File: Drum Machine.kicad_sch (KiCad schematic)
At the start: 20 parts

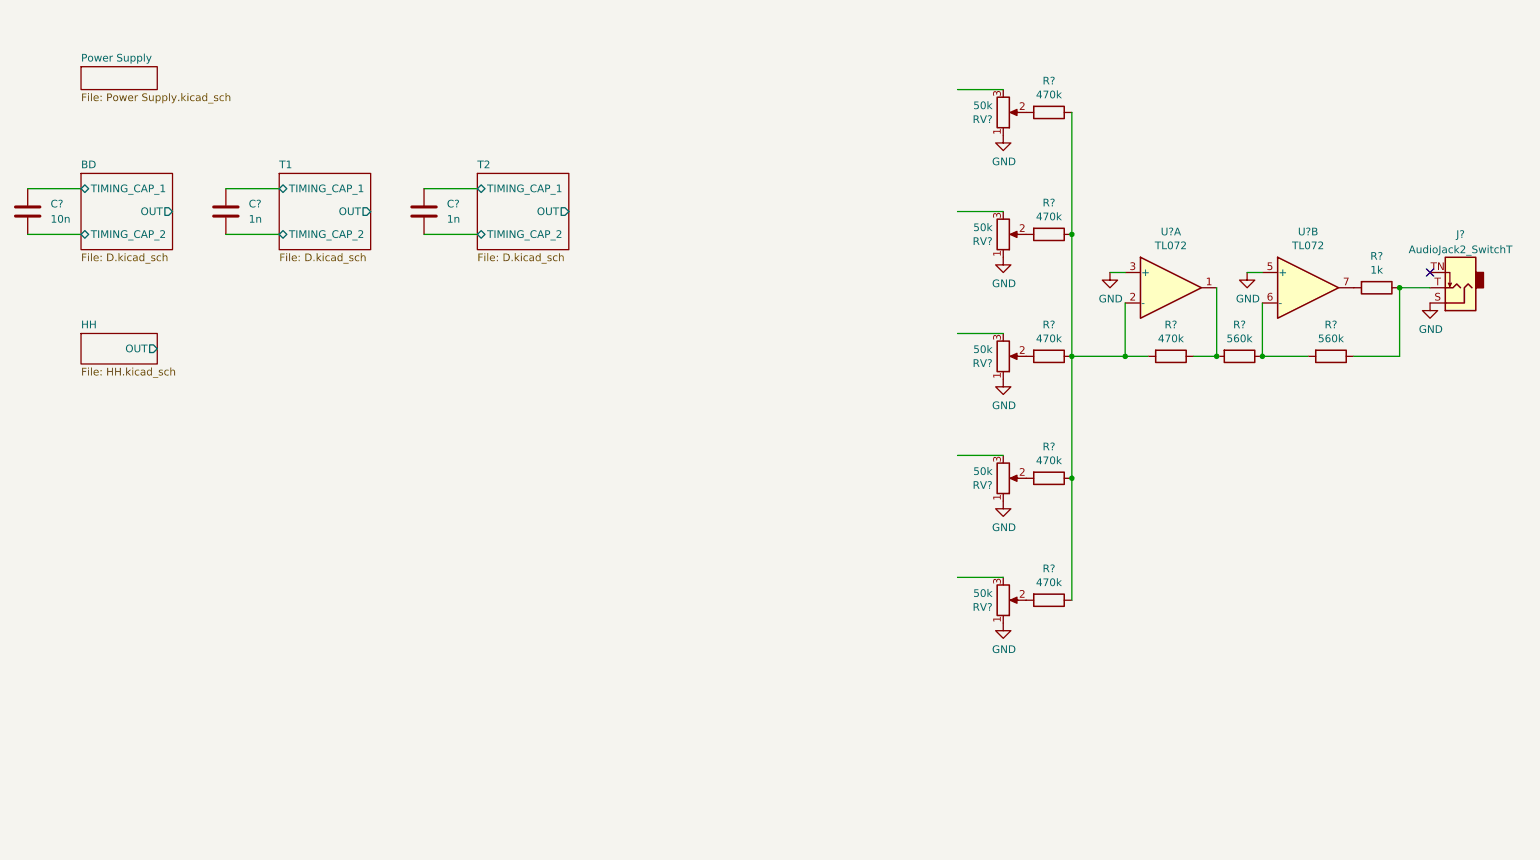
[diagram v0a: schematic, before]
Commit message: Finish schematic
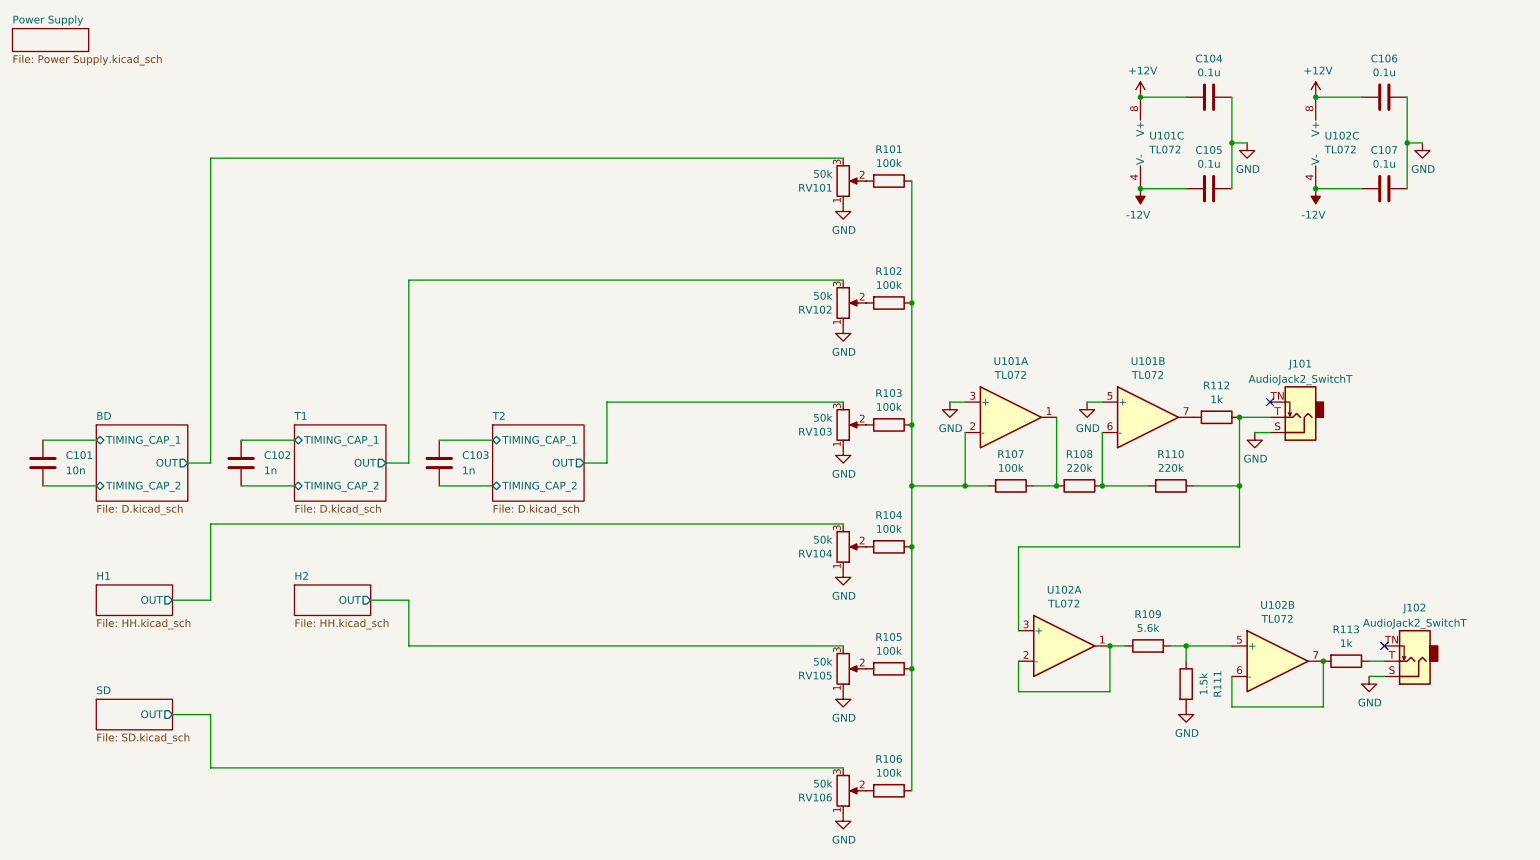
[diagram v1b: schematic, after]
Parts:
- removed R?: 1k, Resistor_THT:R_Axial_DIN0207_L6.3mm_D2.5mm_P7.62mm_Horizontal, symbol Device:R
- added C104, C105, C106, C107: 0.1u, Capacitor_THT:C_Disc_D5.0mm_W2.5mm_P5.00mm, symbol Device:C
- added J102: AudioJack2_SwitchT, Connector_Audio:Jack_3.5mm_QingPu_WQP-PJ398SM_Vertical_CircularHoles, symbol Connector:AudioJack2_SwitchT
- added R106: 100k, Resistor_THT:R_Axial_DIN0207_L6.3mm_D2.5mm_P7.62mm_Horizontal, symbol Device:R
- added R109: 5.6k, Resistor_THT:R_Axial_DIN0207_L6.3mm_D2.5mm_P7.62mm_Horizontal, symbol Device:R
- added R111: 1.5k, Resistor_THT:R_Axial_DIN0207_L6.3mm_D2.5mm_P7.62mm_Horizontal, symbol Device:R
- added R112, R113: 1k, Resistor_THT:R_Axial_DIN0207_L6.3mm_D2.5mm_P7.62mm_Horizontal, symbol Device:R
- added RV106: 50k, Potentiometer_THT:Potentiometer_Alpha_RD901F-40-00D_Single_Vertical_CircularHoles, symbol Device:R_Potentiometer
- added unit 3 of U101
- added U102: TL072, Package_DIP:DIP-8_W7.62mm_Socket, symbol Amplifier_Operational:TL072
- C101, C102, C103: renamed from C?; footprint (none) -> Capacitor_THT:C_Disc_D5.0mm_W2.5mm_P5.00mm
- R101, R102, R103, R104, R105, R107: renamed from R?; value 470k -> 100k
- R108, R110: renamed from R?; value 560k -> 220k
- gave numbers to parts that had none: 7
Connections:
- net BD/OUT: now also RV101.3
- net GND: now also C104.2, C105.2, C106.2, C107.2, J102.S, R111.2, RV106.1
- net H1/OUT: now also RV104.3
- net T1/OUT: now also RV102.3
- net T2/OUT: now also RV103.3
- net at J101.T, R110.1: now also R112.1, U102.3 (+)
- net at U101.7: now also R112.2
- net at R101.1, R102.1, R103.1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: now also R106.1
- net H2/OUT: now reaches RV105.3
- new net: R109.1, U102.1, U102.2 (-)
- new net: J102.T, R113.1
- new net: R113.2, U102.6 (-), U102.7
- new net: R109.2, R111.1, U102.5 (+)
- new net: R106.2, RV106.2
- new net +12V: C104.1, C106.1, U101.8 (V+), U102.8 (V+)
- new net -12V: C105.1, C107.1, U101.4 (V-), U102.4 (V-)
- new net SD/OUT: RV106.3
- no-connect marks 1 -> 2
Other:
- sheet HH renamed H1
- added sheet H2 (HH.kicad_sch)
- added sheet SD (SD.kicad_sch)
- moved on the sheet: C101, C102, C103, J101, R101, R102, R103, R104, R105, R107, R108, R110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

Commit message: Update VCO
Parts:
- removed C101: 10n, Capacitor_THT:C_Disc_D5.0mm_W2.5mm_P5.00mm, symbol Device:C
- removed C102, C103: 1n, Capacitor_THT:C_Disc_D5.0mm_W2.5mm_P5.00mm, symbol Device:C
- renumbered C104 to C101, C105 to C102, C106 to C103, C107 to C104
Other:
- sheet BD ports: added none; removed TIMING_CAP_1, TIMING_CAP_2
- sheet T1 ports: added none; removed TIMING_CAP_1, TIMING_CAP_2
- sheet T2 ports: added none; removed TIMING_CAP_1, TIMING_CAP_2

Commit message: Finish PCB
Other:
- sheet BD renamed D1
- sheet T1 renamed D2
- sheet T2 renamed D3
